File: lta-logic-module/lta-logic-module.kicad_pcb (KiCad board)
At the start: 2 copper layers, 125 x 89.5 mm, 83 parts, among them J1 Molex-MicroFit_43650-0218, J2 Molex-MicroLatch-53253-1270, J3 Molex-MicroLatch-53253-1270, J4 Molex-MicroLatch-53253-1270, Q1 PT334-6B, Q2 2N3904, SW1 SW_SPST, U1 Feather_M4_Express, U10 SN74LVC00AD, U11 SN74LVC14AD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

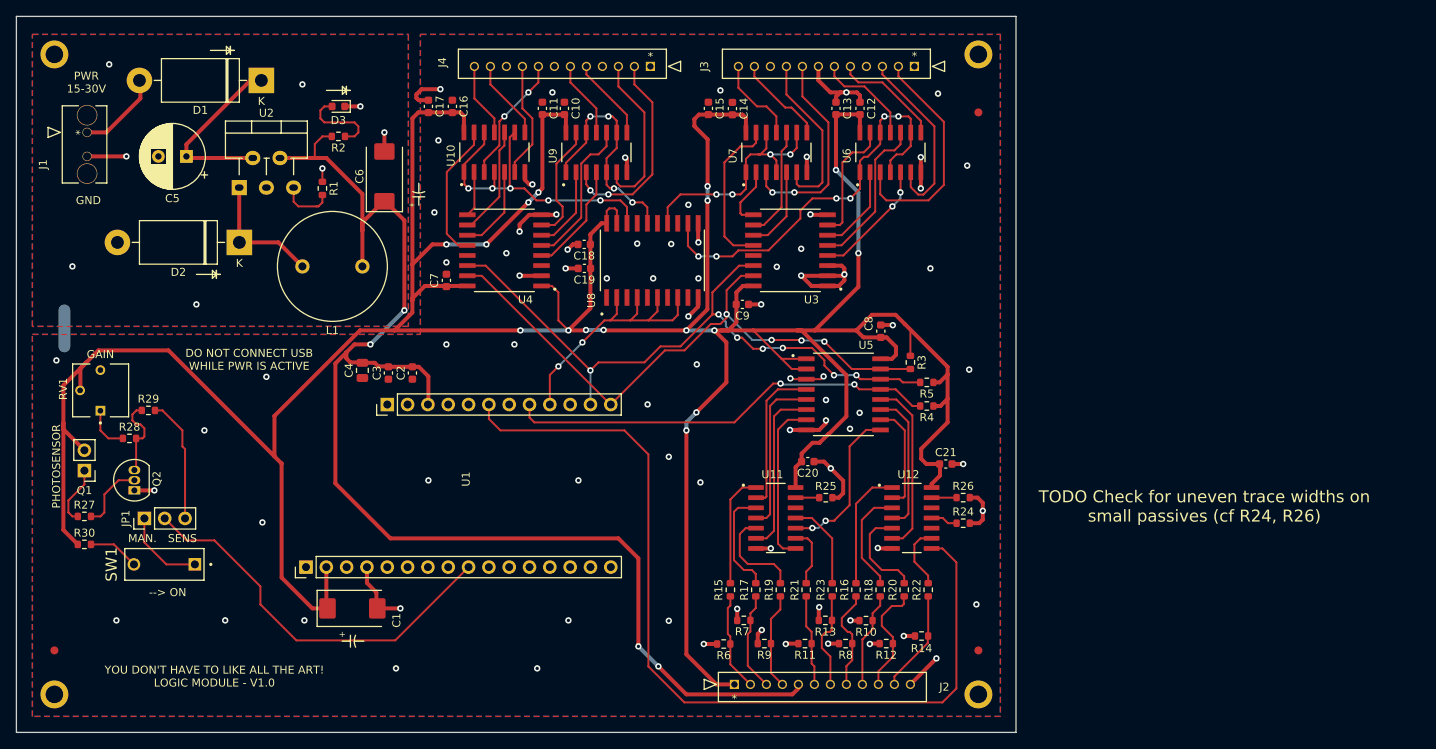
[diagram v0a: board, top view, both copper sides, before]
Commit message: Relocated optosensor to south side of board.
* Moved optosensor logic away from the USB plug-side of the Feather.
  You can now plug in USB while the Feather is attached to the board.
* Changed schematic such that `button0` now goes directly to the
  Feather; buttons 1--8 are on the I2C bus. Cleans up some obnoxious
  routing.
* Optimized other routing & GND fill.
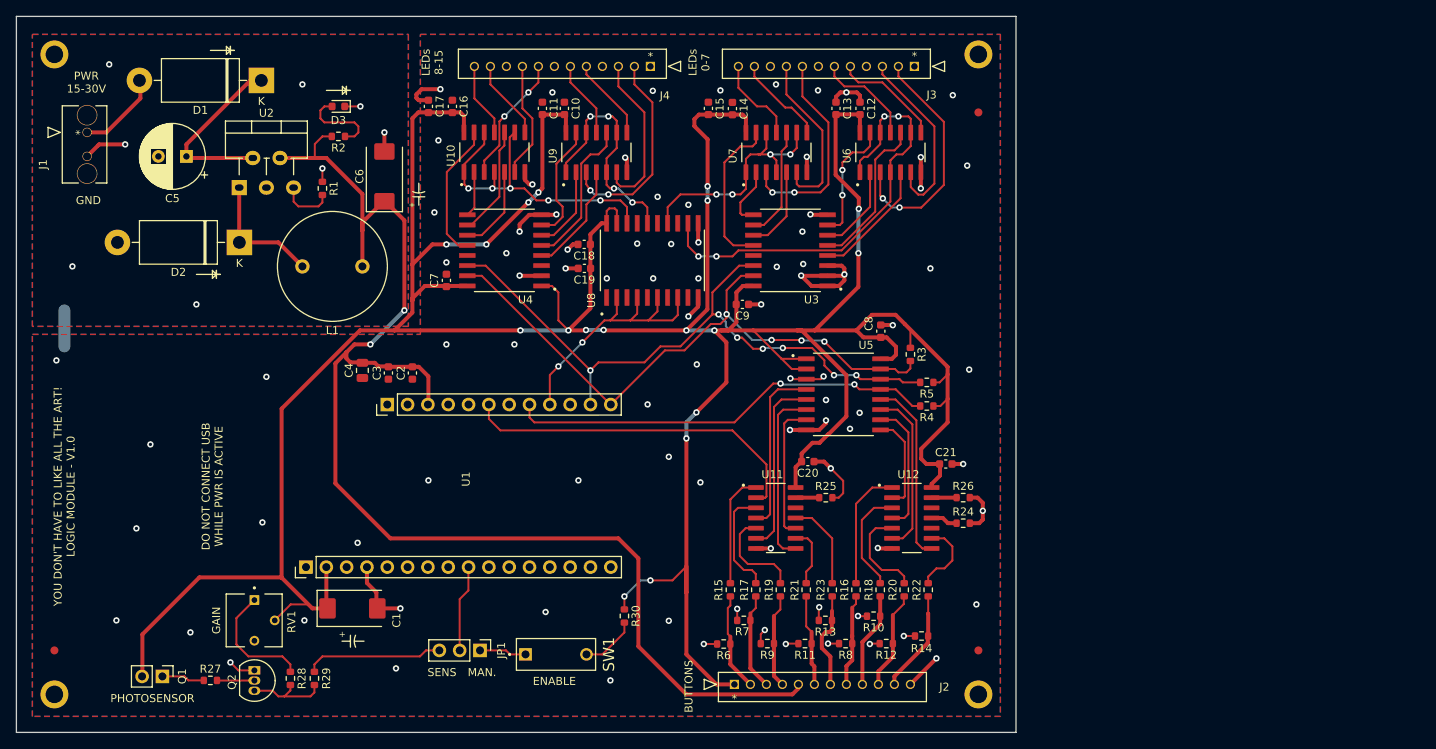
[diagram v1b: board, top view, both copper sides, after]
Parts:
- moved R30 68.1 mm to (93.0, 92.5), turned to -90 degrees
- moved SW1 50.2 mm to (84.5, 97.2), turned to -90 degrees
- moved JP1 45.1 mm to (75.0, 96.7), turned to -90 degrees
- moved R29 39.4 mm to (54.3, 100.2), turned to 90 degrees
- moved R28 36.1 mm to (51.3, 100.2), turned to -90 degrees
- moved RV1 34.6 mm to (46.8, 93.0), turned to -90 degrees
- moved Q1 27.5 mm to (35.3, 100.0), turned to -90 degrees
- moved Q2 27.0 mm to (46.8, 99.2), turned to -90 degrees
- moved R27 25.9 mm to (41.3, 100.5)
- moved R10 1.10 mm to (124.2, 92.5)
- moved R3 1.00 mm to (128.8, 59.8)
- moved R9 0.38 mm to (110.9, 95.9)
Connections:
- U1 pad 23: /button8 -> /button0
- U5 pad 10: /button5 -> /button6
- U5 pad 11: /button6 -> /button7
- U5 pad 12: /button7 -> /button8
- U5 pad 4: /button0 -> /button1
- U5 pad 5: /button1 -> /button2
- U5 pad 6: /button2 -> /button3
- U5 pad 7: /button3 -> /button4
- U5 pad 9: /button4 -> /button5
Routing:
- net /button8: track 110.7 -> 23.0 mm
- net /DARK: track 49.4 -> 11.0 mm
- net /button0: track 18.9 -> 44.2 mm
- net +3V3: track 499.6 -> 481.1 mm, vias 16 -> 18
- net Net-(R28-Pad1): track 5.62 -> 15.2 mm
- net Net-(JP1-Pad1): track 10.4 -> 5.90 mm
- net /LED Signal Outputs/EN0_L: track 51.1 -> 55.3 mm, vias 6 -> 4
- net Net-(Q2-Pad2): track 8.61 -> 4.73 mm
- net GND: track 136.0 -> 132.3 mm, vias 89 -> 96
- net /button4: track 20.0 -> 17.3 mm, vias 2 -> 0
- net Net-(Q1-Pad1): track 7.51 -> 5.38 mm
- net /Button Inputs/btn_in7: track 14.1 -> 12.3 mm
- net Net-(JP1-Pad3): track 15.6 -> 17.3 mm
- net /button3: track 20.7 -> 22.4 mm
- net /Button Inputs/btn_buf8: track 8.03 -> 9.46 mm
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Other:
- board text added: "BUTTONS"
- board text added: "ENABLE"
- board text added: "LEDs 0-7"
- board text added: "LEDs 8-15"
- board text removed: "--> ON"
- board text removed: "<<< PROCESS DIRECTION >>>"
- board text removed: "TODO Check for uneven trace widths on small passives (cf R24, R26)"

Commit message: Add test points
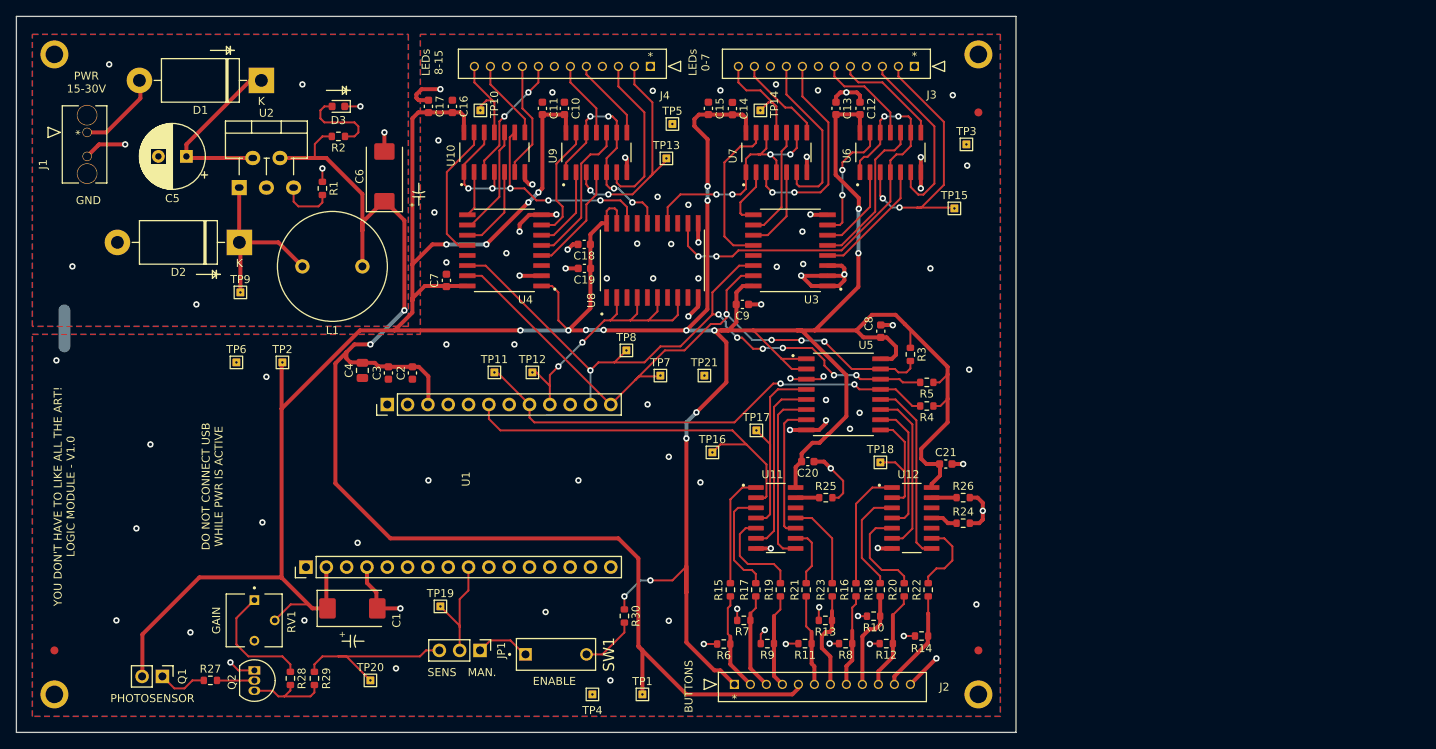
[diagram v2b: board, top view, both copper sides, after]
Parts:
- added TP1: TestPoint_Flag, Aaron_THT:TestPoint_THTPad_1.0x1.0mm_Drill0.3mm, F.Cu at (95.3, 102.2)
- added TP10: TestPoint_Flag, Aaron_THT:TestPoint_THTPad_1.0x1.0mm_Drill0.3mm, F.Cu at (75.0, 29.2)
- added TP11: TestPoint_Flag, Aaron_THT:TestPoint_THTPad_1.0x1.0mm_Drill0.3mm, F.Cu at (76.8, 62.0)
- added TP12: TestPoint_Flag, Aaron_THT:TestPoint_THTPad_1.0x1.0mm_Drill0.3mm, F.Cu at (81.5, 62.0)
- added TP13: TestPoint_Flag, Aaron_THT:TestPoint_THTPad_1.0x1.0mm_Drill0.3mm, F.Cu at (98.3, 35.2)
- added TP14: TestPoint_Flag, Aaron_THT:TestPoint_THTPad_1.0x1.0mm_Drill0.3mm, F.Cu at (110.0, 29.2)
- added TP15: TestPoint_Flag, Aaron_THT:TestPoint_THTPad_1.0x1.0mm_Drill0.3mm, F.Cu at (134.3, 41.5)
- added TP16: TestPoint_Flag, Aaron_THT:TestPoint_THTPad_1.0x1.0mm_Drill0.3mm, F.Cu at (104.0, 72.0)
- added TP17: TestPoint_Flag, Aaron_THT:TestPoint_THTPad_1.0x1.0mm_Drill0.3mm, F.Cu at (109.5, 69.2)
- added TP18: TestPoint_Flag, Aaron_THT:TestPoint_THTPad_1.0x1.0mm_Drill0.3mm, F.Cu at (125.0, 73.2)
- added TP19: TestPoint_Flag, Aaron_THT:TestPoint_THTPad_1.0x1.0mm_Drill0.3mm, F.Cu at (70.0, 91.2)
- added TP2: TestPoint_Flag, Aaron_THT:TestPoint_THTPad_1.0x1.0mm_Drill0.3mm, F.Cu at (50.3, 60.8)
- added TP20: TestPoint_Flag, Aaron_THT:TestPoint_THTPad_1.0x1.0mm_Drill0.3mm, F.Cu at (61.3, 100.5)
- added TP21: TestPoint_Flag, Aaron_THT:TestPoint_THTPad_1.0x1.0mm_Drill0.3mm, F.Cu at (103.0, 62.4)
- added TP3: TestPoint_Flag, Aaron_THT:TestPoint_THTPad_1.0x1.0mm_Drill0.3mm, F.Cu at (135.8, 33.5)
- added TP4: TestPoint_Flag, Aaron_THT:TestPoint_THTPad_1.0x1.0mm_Drill0.3mm, F.Cu at (89.0, 102.2)
- added TP5: TestPoint_Flag, Aaron_THT:TestPoint_THTPad_1.0x1.0mm_Drill0.3mm, F.Cu at (99.0, 30.9)
- added TP6: TestPoint_Flag, Aaron_THT:TestPoint_THTPad_1.0x1.0mm_Drill0.3mm, F.Cu at (44.5, 60.8)
- added TP7: TestPoint_Flag, Aaron_THT:TestPoint_THTPad_1.0x1.0mm_Drill0.3mm, F.Cu at (97.5, 62.4)
- added TP8: TestPoint_Flag, Aaron_THT:TestPoint_THTPad_1.0x1.0mm_Drill0.3mm, F.Cu at (93.3, 59.2)
- added TP9: TestPoint_Flag, Aaron_THT:TestPoint_THTPad_1.0x1.0mm_Drill0.3mm, F.Cu at (45.0, 52.0)
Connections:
- net Net-(JP1-Pad3) renamed /Light-level sensor/DARK_SENS
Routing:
- net VDD: track 162.2 -> 168.4 mm
- net /5V0 (1A) Regulator/VOUT: track 15.9 -> 21.9 mm
- net /BUTTON_INT_L: track 53.9 -> 59.6 mm
- net /Light-level sensor/DARK_SENS: track 17.3 -> 22.5 mm
- net +3V3: track 481.1 -> 485.9 mm
- net /LED Signal Outputs/s0: track 29.9 -> 34.7 mm
- net /button0: track 44.2 -> 48.9 mm
- net /DARK: track 11.0 -> 14.5 mm
- net /button5: track 12.1 -> 15.7 mm
- net /SDA: track 78.2 -> 81.7 mm
- net /button1: track 21.5 -> 24.7 mm
- net /LED_EN_L: track 34.7 -> 37.6 mm
- net /LED Signal Outputs/s8: track 25.9 -> 28.7 mm
- net /LED Signal Outputs/s15: track 9.29 -> 11.6 mm
- net /LED Signal Outputs/s7: track 10.9 -> 13.2 mm
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
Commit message: Final tweaks before RTM.
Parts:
- moved D2 2.30 mm to (44.9, 43.5)
- moved TP19 1.82 mm to (69.5, 93.0)
- moved C5 1.77 mm to (37.6, 33.4), turned to -90 degrees
- moved C1 1.35 mm to (59.1, 92.8)
- moved R15 0.80 mm to (105.5, 89.2)
- moved R17 0.80 mm to (108.7, 89.2)
- moved R19 0.80 mm to (111.8, 89.2)
- moved R7 0.10 mm to (107.9, 93.0)
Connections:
- net /LED Signal Outputs/EN0_L renamed /LED Signal Outputs/EN0
- net /LED Signal Outputs/EN1_L renamed /LED Signal Outputs/EN1
- net /LED Signal Outputs/EN2_L renamed /LED Signal Outputs/EN2
- net /LED_EN_L renamed /LED_EN
- U10 pad 1: /LED Signal Outputs/EN3_L -> /led12
- U10 pad 12: /LED Signal Outputs/EN3_L -> /LED Signal Outputs/EN3
- U10 pad 2: /led12 -> /LED Signal Outputs/EN3
- U10 pad 4: /LED Signal Outputs/EN3_L -> /LED Signal Outputs/EN3
- U10 pad 9: /LED Signal Outputs/EN3_L -> /LED Signal Outputs/EN3
- U8 pad 18: /LED Signal Outputs/EN3_L -> /LED Signal Outputs/EN3
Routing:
- net /LED Signal Outputs/EN3_L: track 40.8 -> 0.00 mm, vias 5 -> 0
- net /LED Signal Outputs/EN3: track 0.00 -> 38.9 mm, vias 0 -> 4
- net +3V3: track 485.9 -> 488.6 mm, vias 18 -> 16
- net /led3: track 15.5 -> 16.7 mm, vias 2 -> 0
- net /5V0 (1A) Regulator/VOUT: track 21.9 -> 23.0 mm
- net /led7: track 19.6 -> 20.6 mm
- net /Button Inputs/btn_buf2: track 12.5 -> 11.5 mm
- net GND: track 132.1 -> 133.0 mm
- net /SCL: track 84.9 -> 85.9 mm, vias 7 -> 5
- net /Button Inputs/btn_buf1: track 13.6 -> 12.8 mm
- net /LED Signal Outputs/EN2: vias 4 -> 2

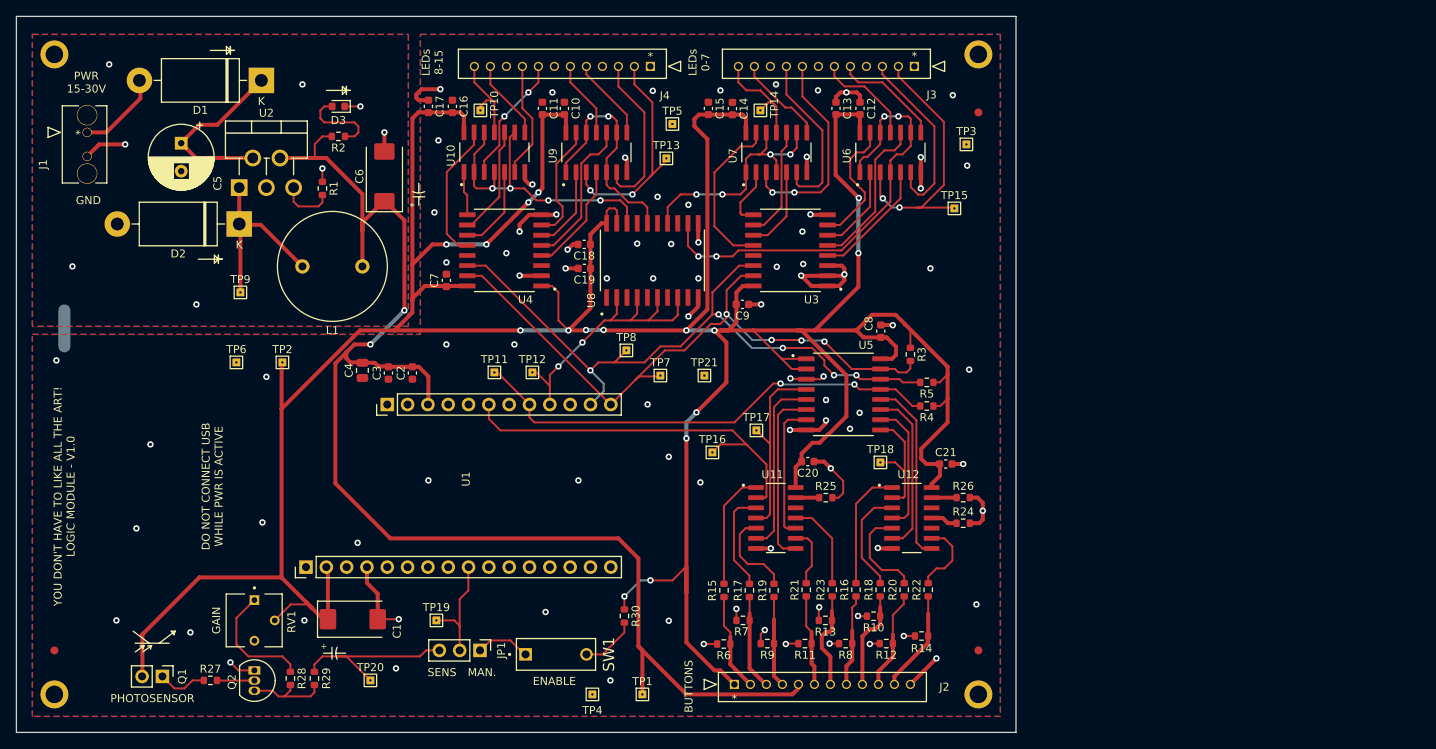
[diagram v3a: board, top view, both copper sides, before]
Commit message: Isolated ground planes for AGND and DGND.
* Analog optosensor now has isolated ground plane area.
* Moved 3V3 load capacitor behind U1 to keep its return
  fully on digital ground.
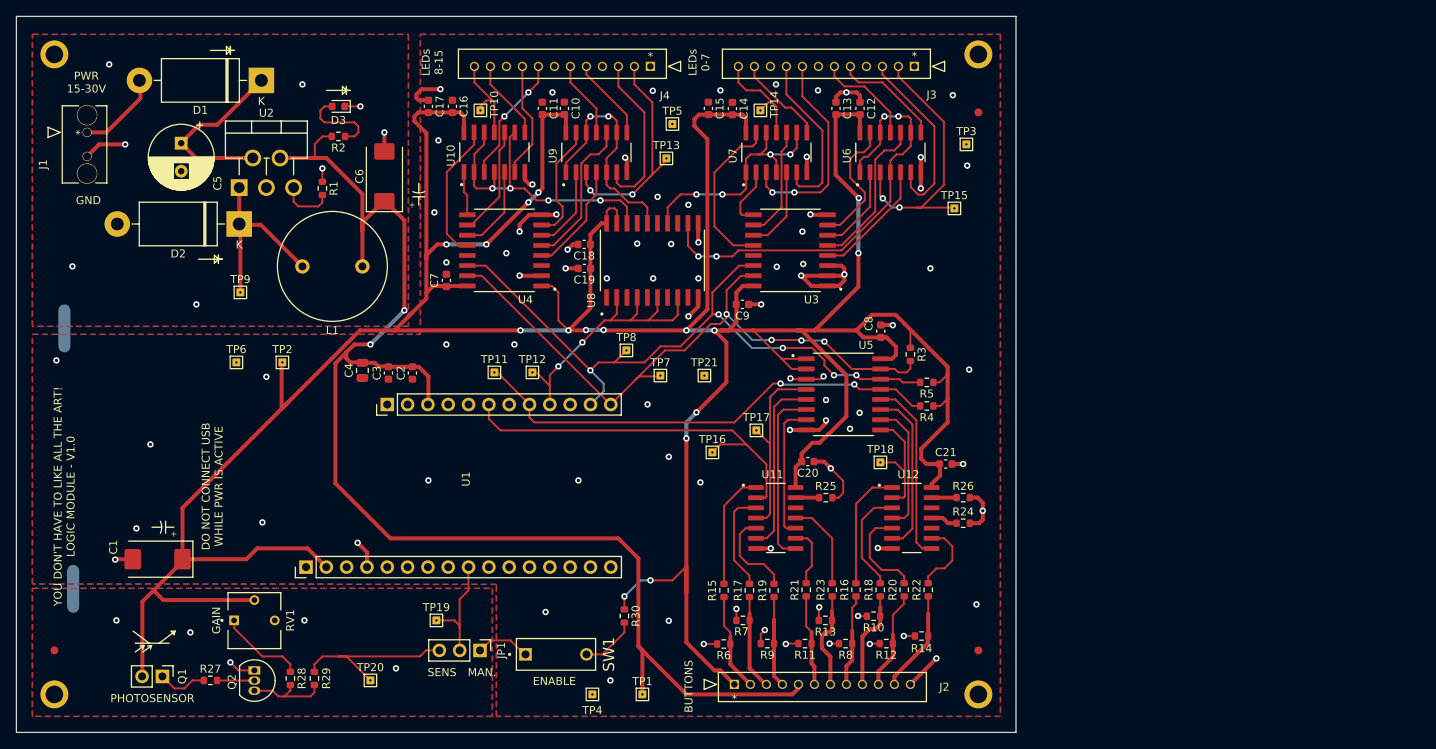
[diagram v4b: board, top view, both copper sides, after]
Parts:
- moved C1 25.5 mm to (34.7, 85.3), turned to 180 degrees
- turned RV1 to 0 degrees
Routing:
- net +3V3: track 488.6 -> 493.5 mm
- net Net-(R28-Pad1): track 15.2 -> 10.8 mm
- net GND: track 133.0 -> 133.6 mm

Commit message: Fix GND path return.
* Route power traces over ground plane.
* Add routed corners to edge cuts
* Remove final TODO notes.
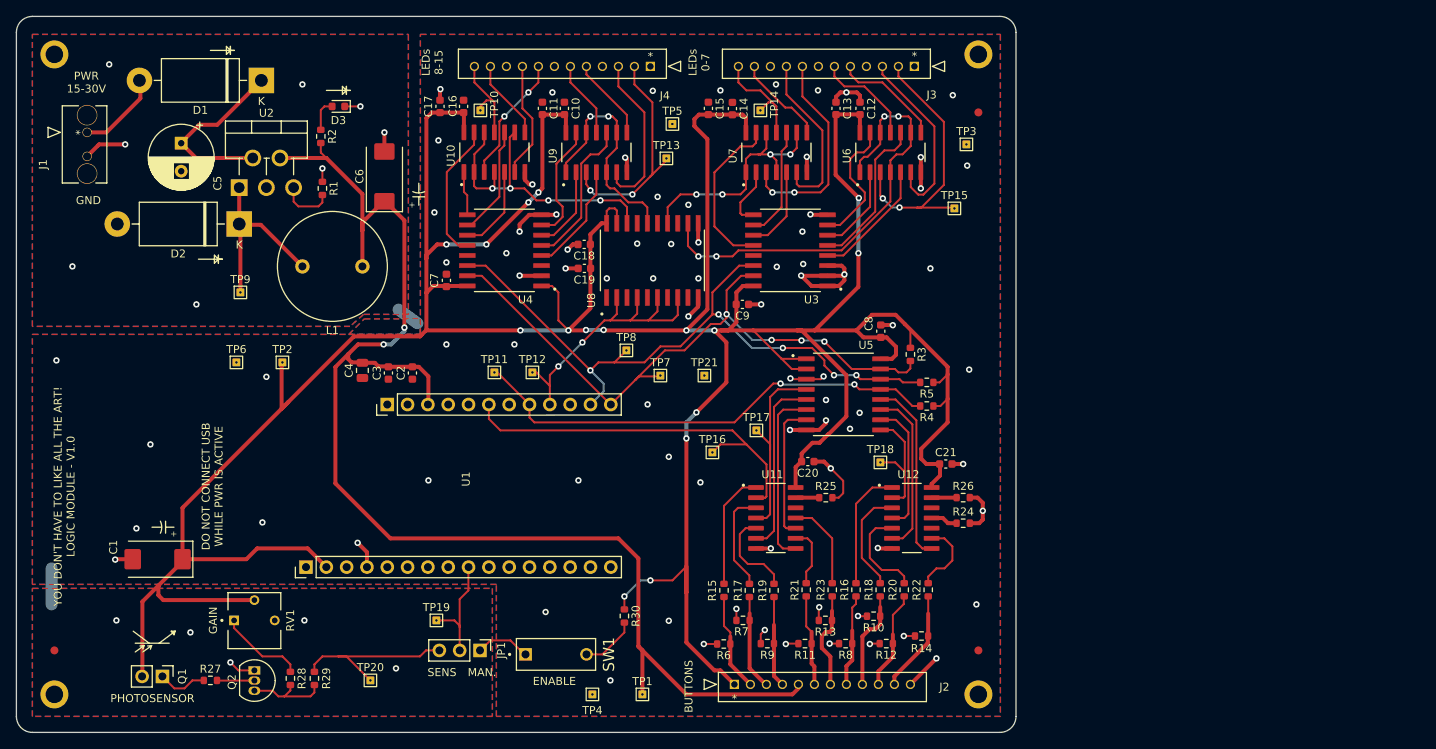
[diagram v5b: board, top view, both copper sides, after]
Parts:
- moved R2 2.20 mm to (55.1, 32.5), turned to -90 degrees
- moved C17 1.45 mm to (70.0, 28.8)
- moved C16 1.40 mm to (73.0, 28.8)
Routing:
- net Net-(D3-Pad2): track 10.5 -> 4.07 mm
- net GND: track 133.6 -> 128.1 mm
- net +3V3: track 493.5 -> 489.0 mm
- net VDD: track 168.4 -> 167.2 mm
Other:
- outline, holes or cut-outs redrawn
